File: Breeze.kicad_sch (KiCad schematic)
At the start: 102 parts

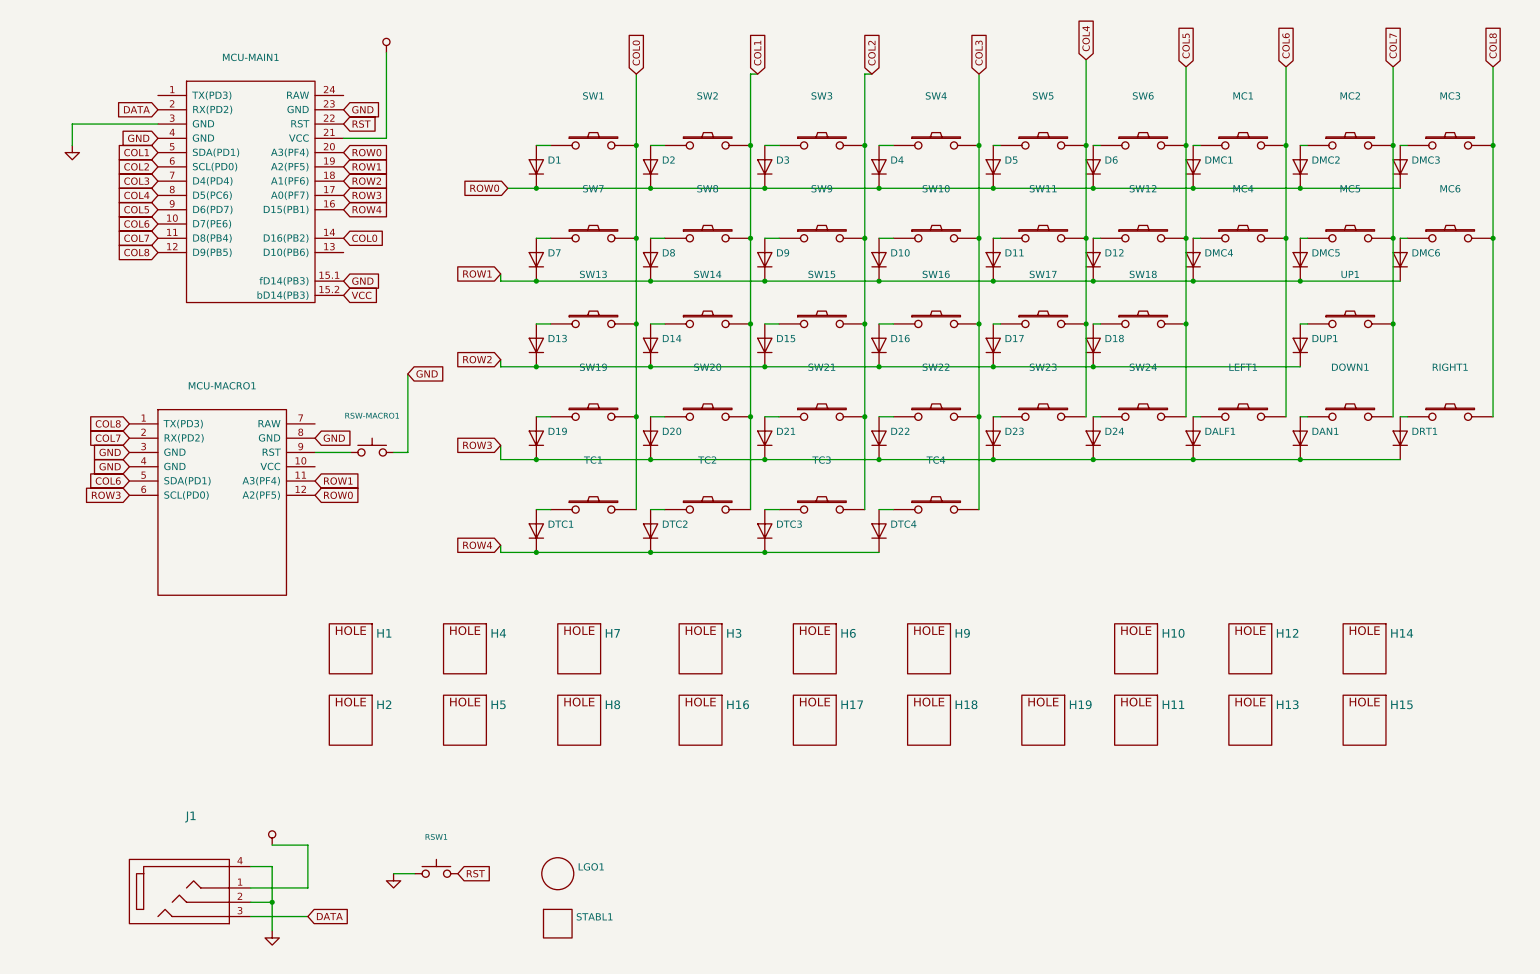
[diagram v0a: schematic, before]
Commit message: added encoder and oled display via elite-pi
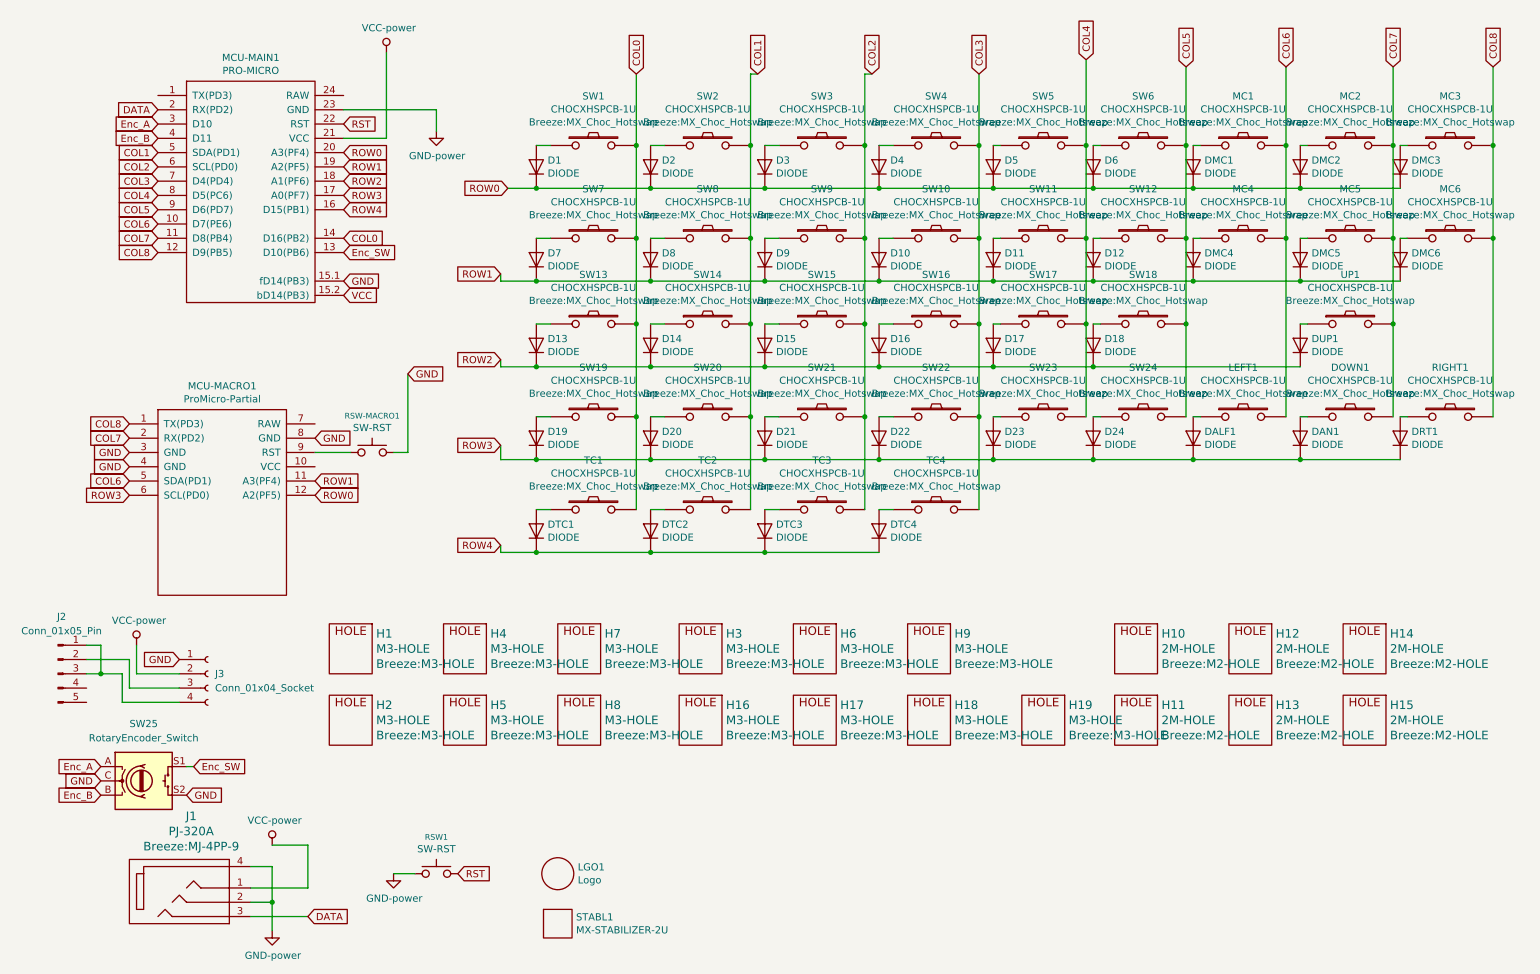
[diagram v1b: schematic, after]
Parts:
- added J2: Conn_01x05_Pin, Connector_PinHeader_2.54mm:PinHeader_1x05_P2.54mm_Vertical, symbol Connector:Conn_01x05_Pin
- added J3: Conn_01x04_Socket, Connector_PinHeader_2.54mm:PinHeader_1x04_P2.54mm_Vertical, symbol Connector:Conn_01x04_Socket
- added SW25: RotaryEncoder_Switch, Rotary_Encoder:RotaryEncoder_Alps_EC11E-Switch_Vertical_H20mm, symbol Device:RotaryEncoder_Switch
- D1, D10, D11, D12, D13, D14, D15, D16, D17, D18, D19, D2, D20, D21, D22, D23, D24, D3, D4, D5, D6, D7, D8, D9, DALF1, DAN1, DMC1, DMC2, DMC3, DMC4, DMC5, DMC6, DRT1, DTC1, DTC2, DTC3, DTC4, DUP1: value (none) -> DIODE; footprint (none) -> Breeze:SOD-123FL
- DOWN1, LEFT1, MC1, MC2, MC3, MC4, MC5, MC6, RIGHT1, SW1, SW10, SW11, SW12, SW13, SW14, SW15, SW16, SW17, SW18, SW19, SW2, SW20, SW21, SW22, SW23, SW24, SW3, SW4, SW5, SW6, SW7, SW8, SW9, TC1, TC2, TC3, TC4, UP1: value (none) -> CHOCXHSPCB-1U; footprint (none) -> Breeze:MX_Choc_Hotswap
- H1, H16, H17, H18, H19, H2, H3, H4, H5, H6, H7, H8, H9: value (none) -> M3-HOLE; footprint (none) -> Breeze:M3-HOLE
- H10, H11, H12, H13, H14, H15: value (none) -> 2M-HOLE; footprint (none) -> Breeze:M2-HOLE
- J1: value (none) -> PJ-320A; footprint (none) -> Breeze:MJ-4PP-9
- LGO1: value (none) -> Logo; footprint (none) -> Breeze:logo
- MCU-MACRO1: value (none) -> ProMicro-Partial; footprint (none) -> Breeze:PROMICRO-PARTIAL2
- MCU-MAIN1: value (none) -> PRO-MICRO; footprint (none) -> Breeze:ProMicro
- RSW-MACRO1, RSW1: value (none) -> SW-RST; footprint (none) -> Breeze:TACT_SWITCH_TVBP06
- STABL1: value (none) -> MX-STABILIZER-2U; footprint (none) -> Breeze:Stabilizer_MX_2u
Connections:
- net GND: now also J3.1 (Pin_1), SW25.C, SW25.S2; no longer MCU-MAIN1.3 (GND), MCU-MAIN1.4 (GND)
- net VCC: now also J3.2 (Pin_2)
- net Enc_SW: now reaches MCU-MAIN1.13 (D10(PB6))
- net Enc_SW: now also SW25.S1
- new net: J2.2 (Pin_2), J3.3 (Pin_3)
- new net: J2.1 (Pin_1), J2.3 (Pin_3), J3.4 (Pin_4)
- new net Enc_A: MCU-MAIN1.3 (GND), SW25.A
- new net Enc_B: MCU-MAIN1.4 (GND), SW25.B
